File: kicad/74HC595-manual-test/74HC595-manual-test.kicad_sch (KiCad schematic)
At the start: 24 parts, among them SW1 SW_Push, SW2 SW_Push, SW3 SW_Push, U1 74HC595

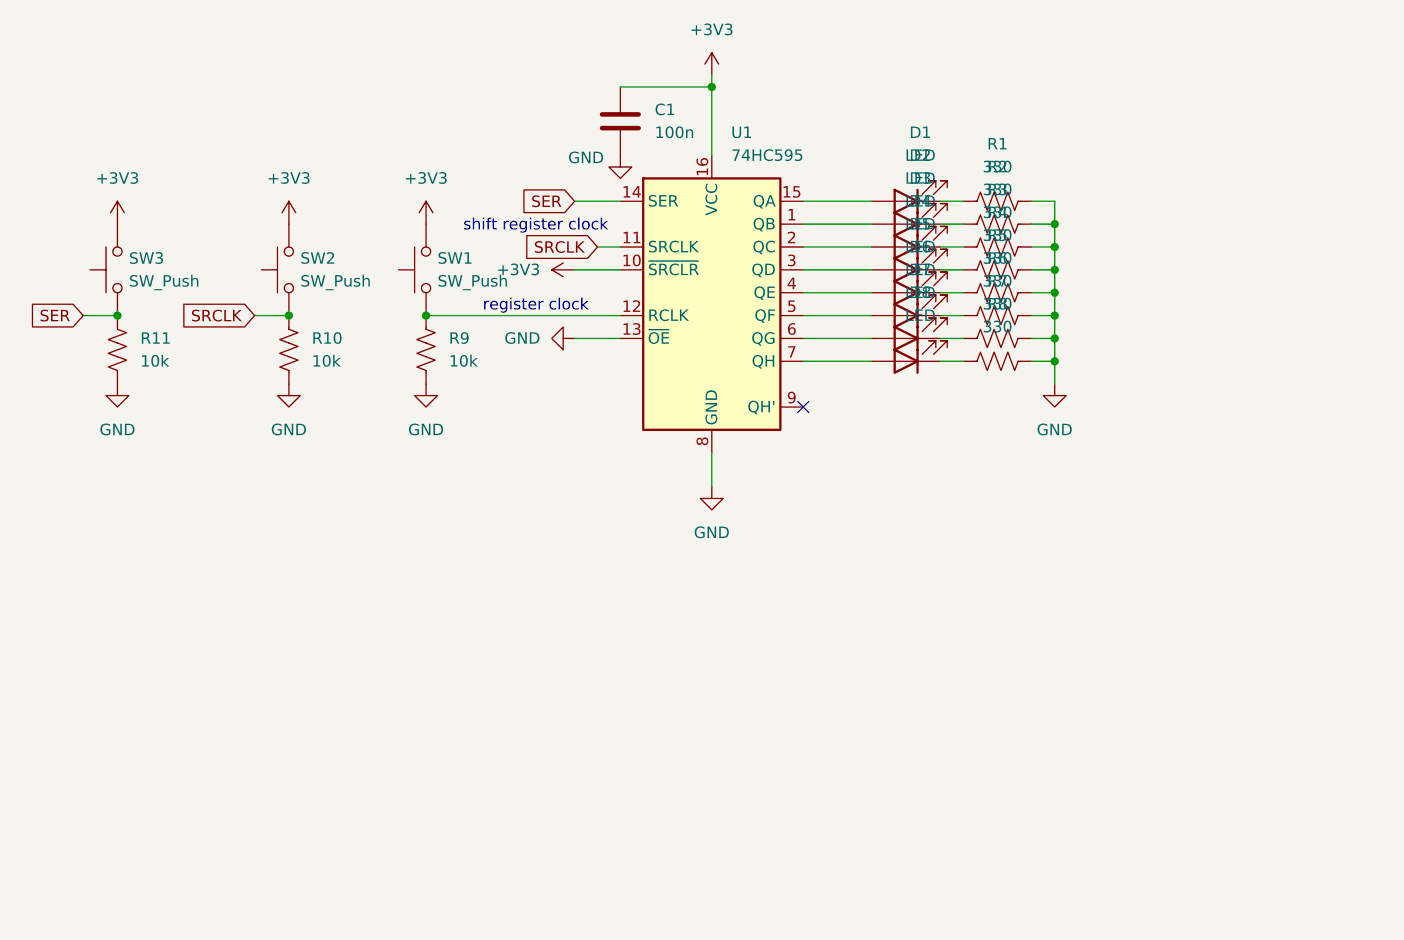
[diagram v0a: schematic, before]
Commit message: KiCad 74HC595 test: LED bank, debounce cap on SRCLK, power flags
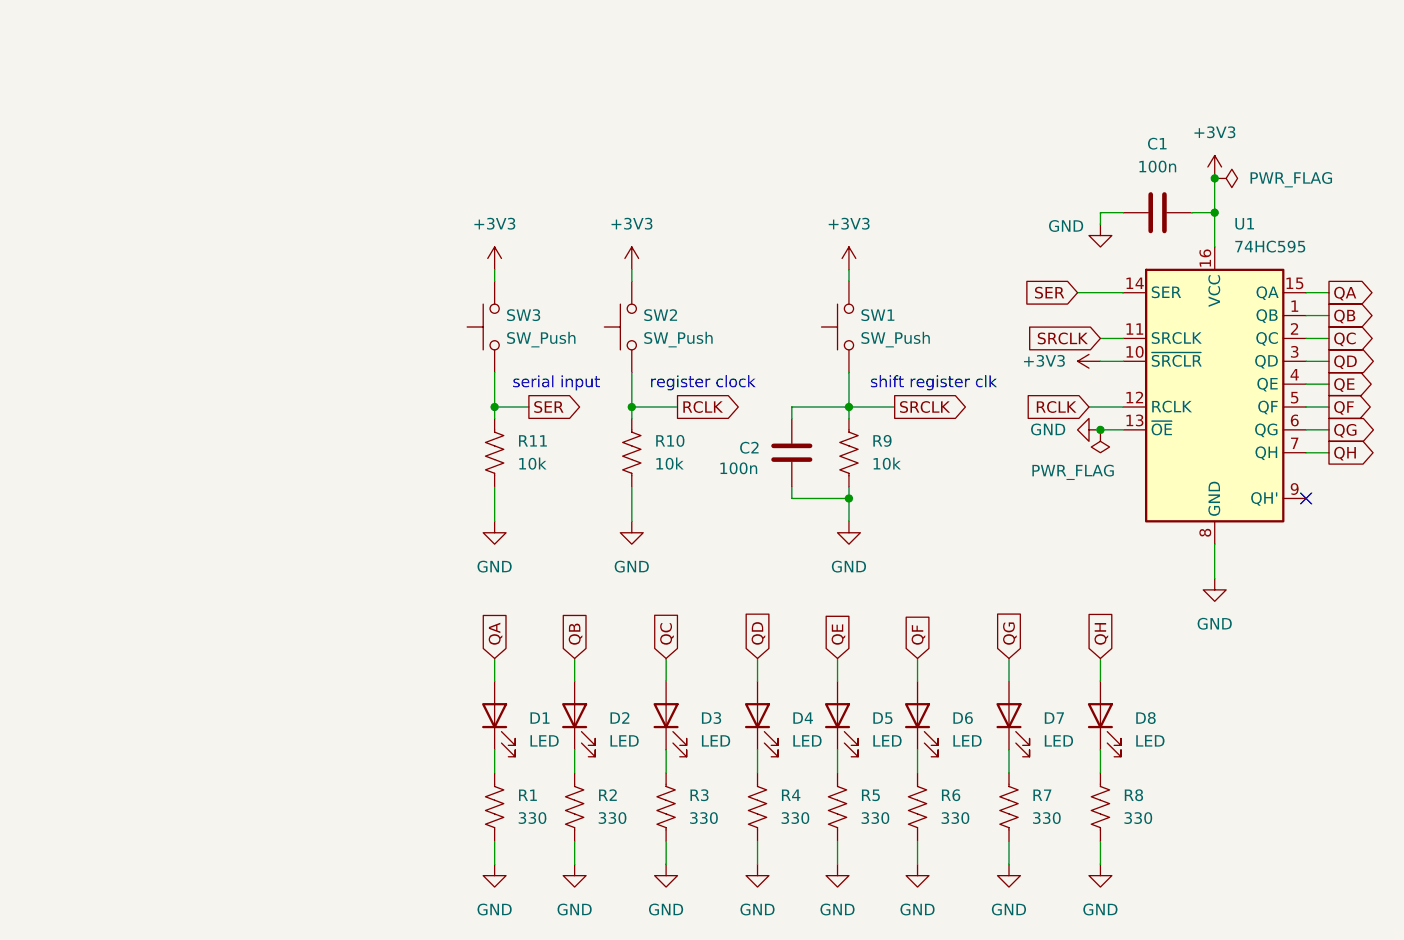
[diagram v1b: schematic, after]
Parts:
- added C2: 100n, symbol Device:C
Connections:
- net +3V3: now also C1.2; no longer C1.1
- net GND: now also C1.1, C2.2; no longer C1.2
- net SRCLK: now also R9.1, SW1.1, C2.1; no longer R10.1, SW2.1
- net QD: now reaches D4.2 (A), U1.3 (QD)
- net QH: now reaches D8.2 (A), U1.7 (QH)
- net QG: now reaches D7.2 (A), U1.6 (QG)
- net QB: now reaches D2.2 (A), U1.1 (QB)
- net QE: now reaches D5.2 (A), U1.4 (QE)
- net QA: now reaches D1.2 (A), U1.15 (QA)
- net QC: now reaches D3.2 (A), U1.2 (QC)
- net QF: now reaches D6.2 (A), U1.5 (QF)
- new net RCLK: R10.1, SW2.1, U1.12 (RCLK)
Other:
- note added: "serial input"
- note added: "shift register clk"
- note removed: "shift register clock"
- moved on the sheet: C1, R10, R11, R9, SW1, SW2, SW3, U1
